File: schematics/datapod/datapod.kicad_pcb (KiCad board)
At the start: 2 copper layers, 152.7 x 152.7 mm, 64 parts, among them J1 Conn_01x02, J2 Conn_02x03_Odd_Even, J3 Conn_01x02, J4 DB9_Female, J5 DB9_Male_MountingHoles, J6 Micro_SD_Card, J7 Conn_02x02_Odd_Even, J8 Conn_01x02_Female, J9 Conn_02x03_Odd_Even, K1 DS2E-SL2-DC5V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

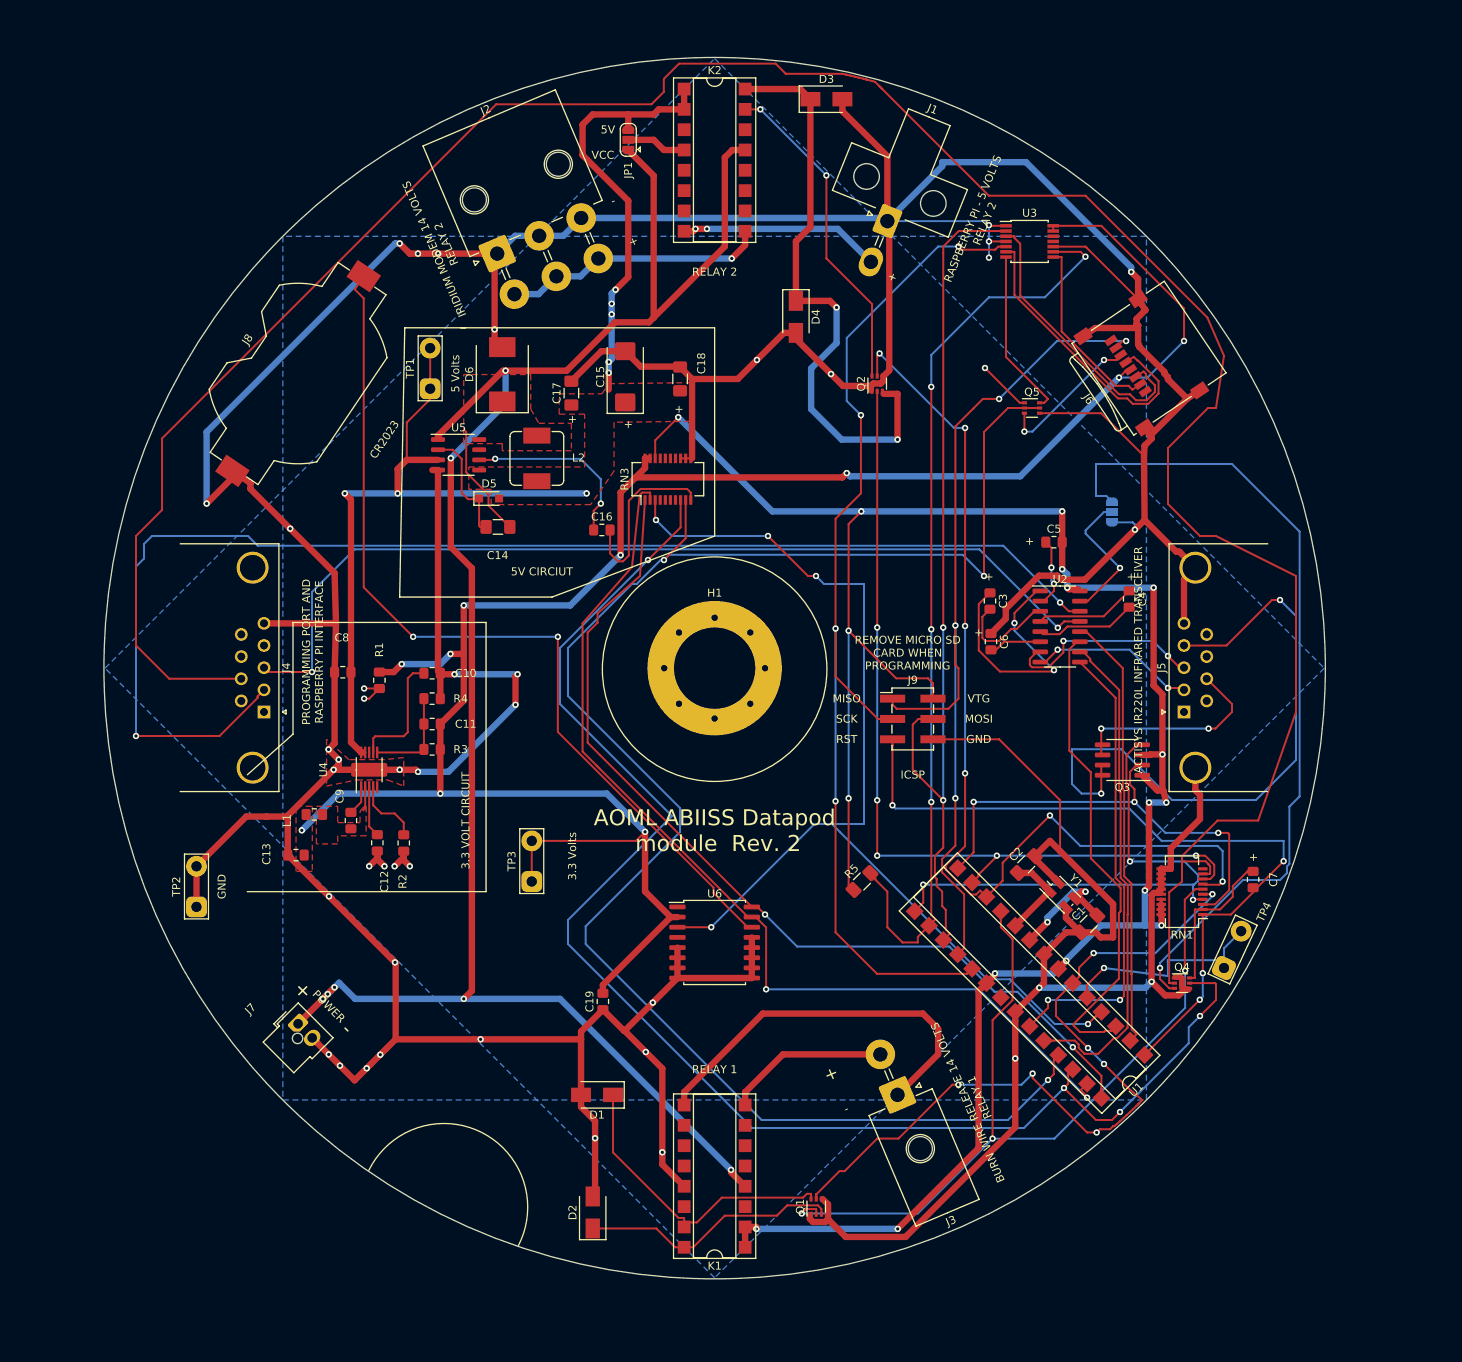
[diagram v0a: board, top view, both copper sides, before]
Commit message: rev 3 , moved db9 connectors out and added ajumper to change output to 14.4v
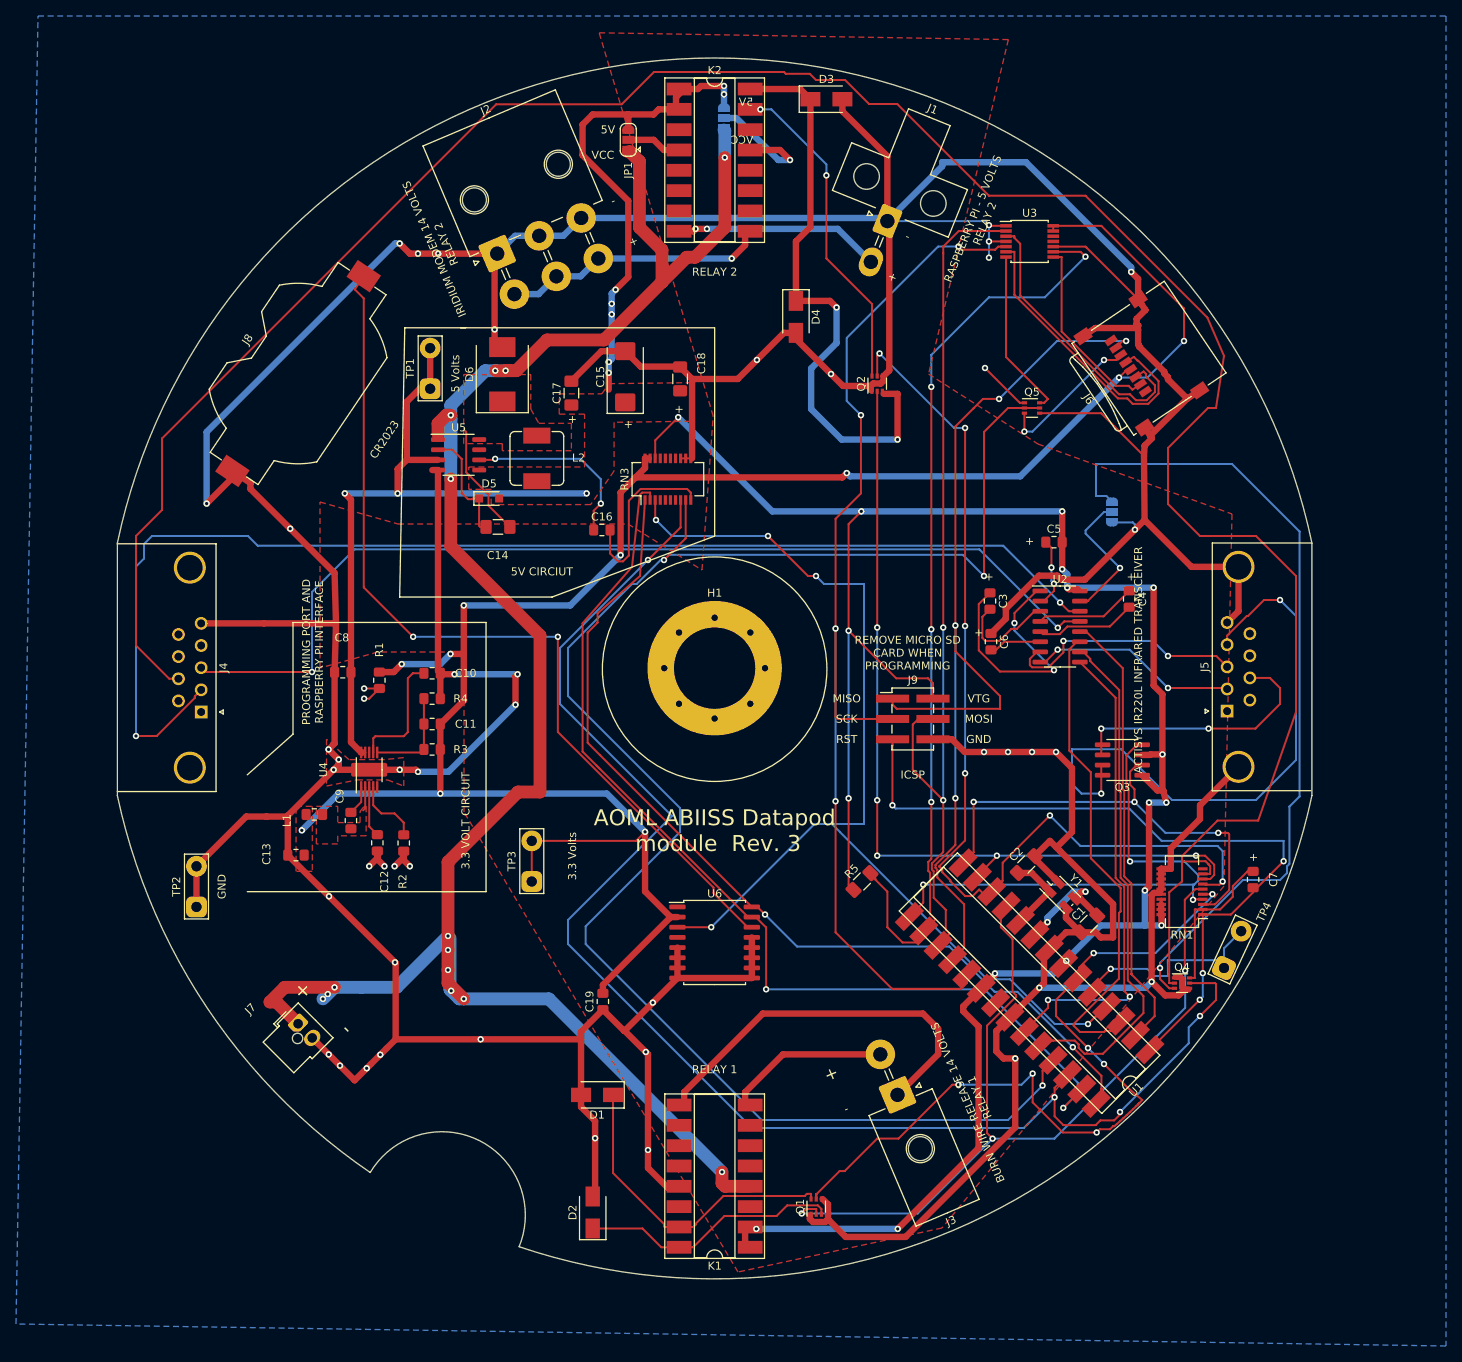
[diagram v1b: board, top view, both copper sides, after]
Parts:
- added JP3: Jumper_3_Open, Jumper:SolderJumper-3_P1.3mm_Open_RoundedPad1.0x1.5mm, B.Cu at (101.5, 27.8)
- K1, K2: footprint Package_DIP:DIP-16_W7.62mm_SMDSocket_SmallPads -> Package_DIP:DIP-16_W8.89mm_SMDSocket_LongPads
- moved J4 7.85 mm to (36.1, 102.0)
- moved J5 5.39 mm to (164.4, 101.9)
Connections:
- K2 pad 13: VCC -> Net-(JP3-Pad2)
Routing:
- net GND: track 905.1 -> 927.5 mm, vias 42 -> 46
- net VCC: track 236.4 -> 258.4 mm, vias 7 -> 14
- net Net-(JP3-Pad2): track 0.00 -> 15.9 mm, vias 0 -> 1
- net +5V: track 425.3 -> 435.5 mm, vias 25 -> 27
- net RTS_PROG: track 318.3 -> 309.0 mm
- net MICRO_SD_MISO: track 115.3 -> 124.0 mm
- net Net-(J4-Pad3): track 118.8 -> 126.7 mm
- net Net-(J4-Pad2): track 164.6 -> 156.8 mm
- net /SERIAL COMMUNICATIONS SHEET/RTS_ON: track 25.9 -> 33.1 mm
- net Net-(J5-Pad3): track 25.6 -> 31.0 mm
- net Net-(J5-Pad2): track 20.7 -> 26.0 mm
- net /SERIAL COMMUNICATIONS SHEET/DTR_ON: track 80.0 -> 75.2 mm
- net MICRO_SD_SCK: track 136.1 -> 140.4 mm
- net MCU-SDA: track 125.8 -> 128.2 mm
- net RS232_DRIVER_ON_OFF: track 182.7 -> 184.6 mm
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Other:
- board size 152.7 x 152.7 mm -> 149.3 x 152.6 mm
- board text added: "AOML ABIISS Datapod module Rev. 3"
- board text removed: "AOML ABIISS Datapod module Rev. 2"
- board text removed: "POWER"

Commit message: added two capacitors
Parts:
- added C20: 6.3v 3300uF, Capacitor_THT:CP_Radial_D10.0mm_P5.00mm, F.Cu at (117.5, 132.7)
- added C21: 6.3v 3300uF, Capacitor_THT:CP_Radial_D10.0mm_P5.00mm, F.Cu at (106.9, 65.9)
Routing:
- net +5V: track 435.5 -> 443.7 mm
- net Net-(D3-Pad1): track 73.9 -> 69.2 mm
- net +3V3: track 268.0 -> 271.5 mm
- net MCU-SCL: track 118.7 -> 119.3 mm
